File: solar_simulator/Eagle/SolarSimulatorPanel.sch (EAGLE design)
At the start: 82 parts, among them U1 Blue Driver, U2 Red Driver, U3 Green Driver, X1 MKDSN1,5/2-5,08

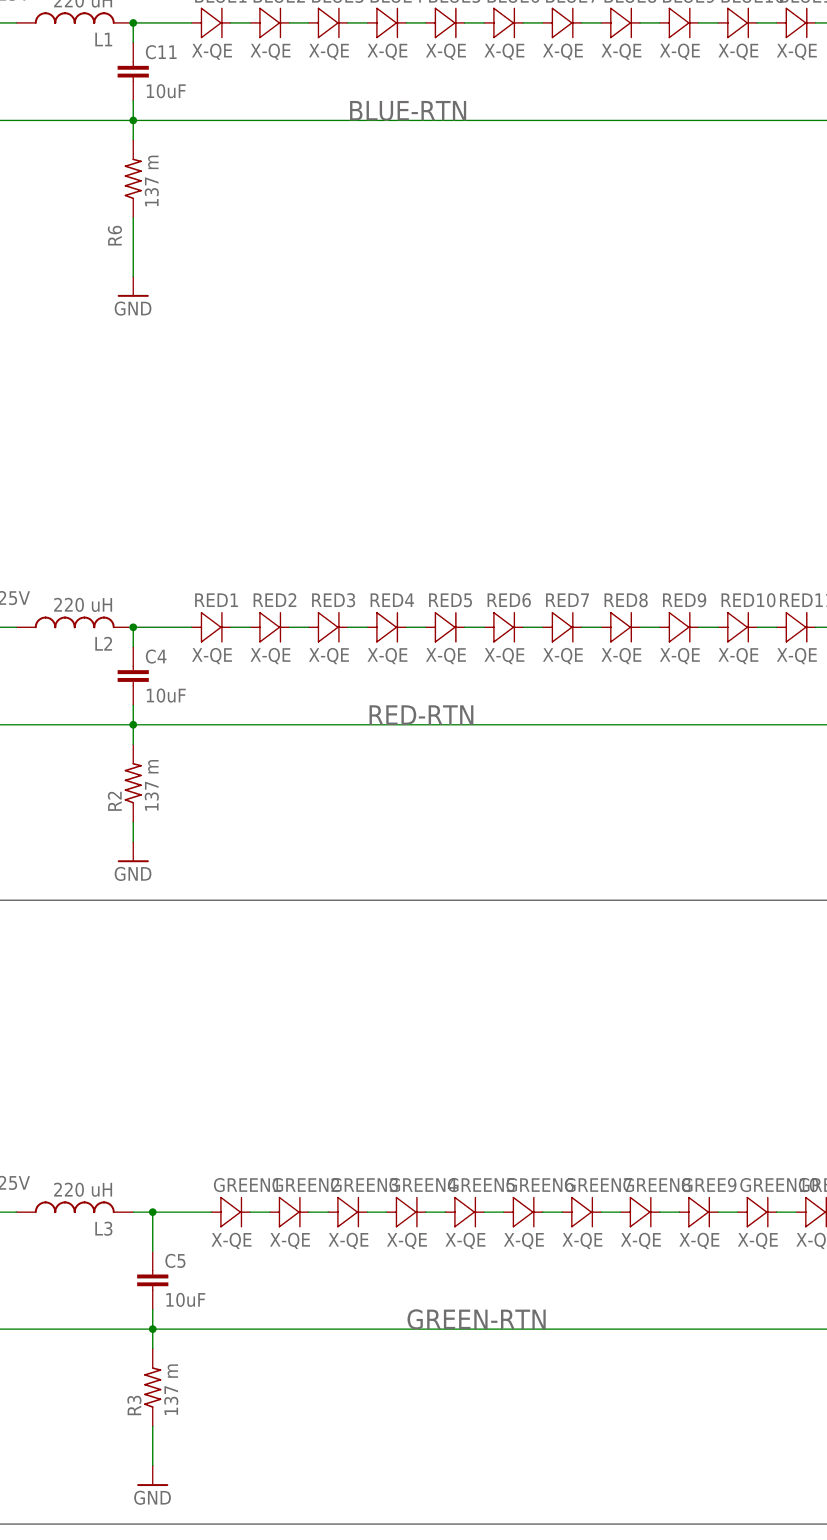
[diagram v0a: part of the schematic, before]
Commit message: added manufacturer informaton for temp sensors on solar sim, tweaks to 1u_panel, added very in progress driver for solar simulator.  Documentation inboud
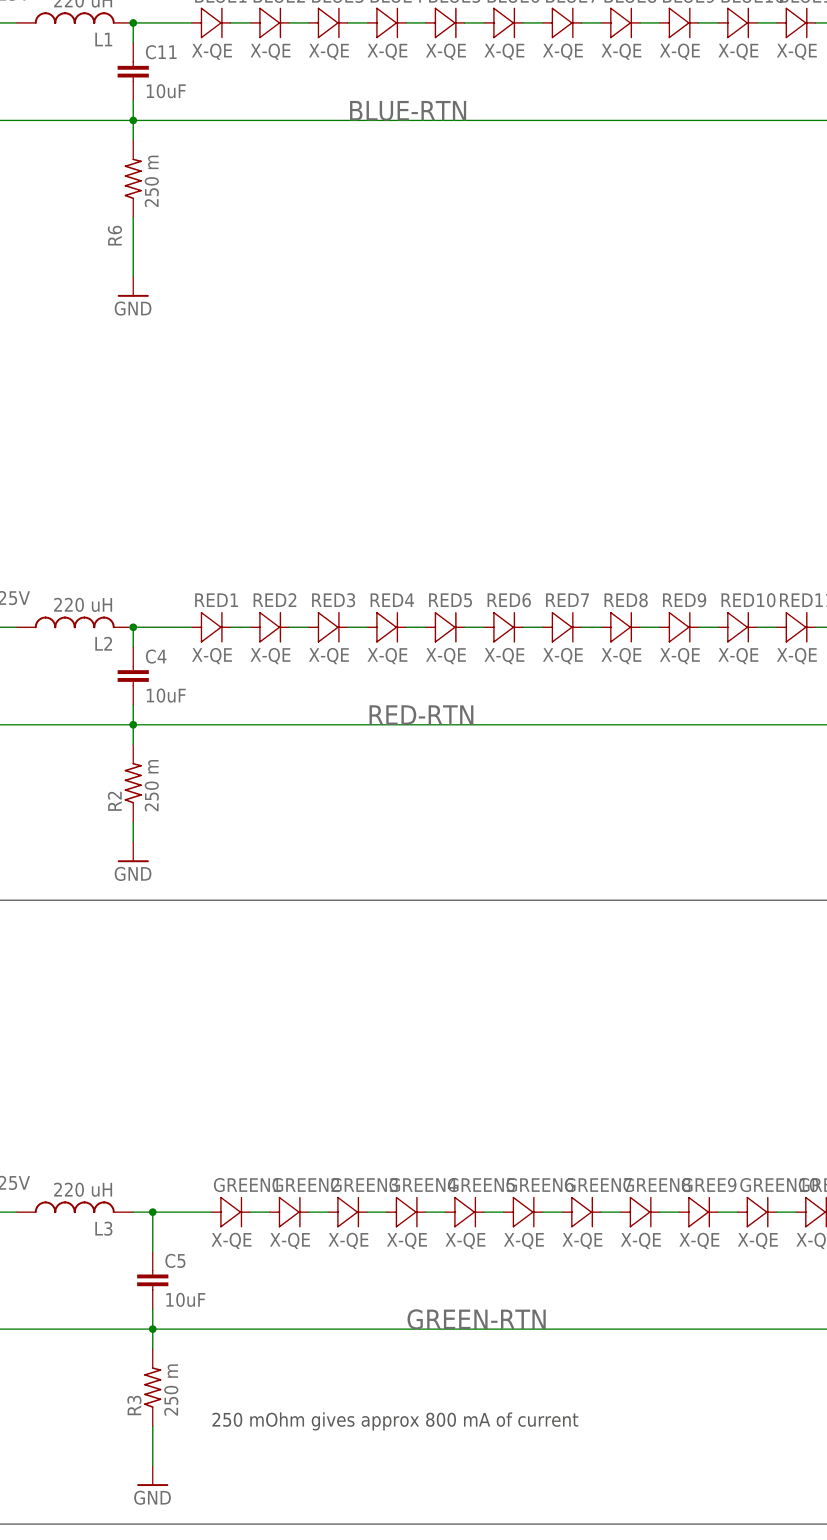
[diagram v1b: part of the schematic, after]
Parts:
- R2, R3, R6: value 137 m -> 250 m
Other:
- note added: "250 mOhm gives approx 800 mA of current"
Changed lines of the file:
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@@
 <?xml version="1.0" encoding="utf-8"?>
 <!DOCTYPE eagle SYSTEM "eagle.dtd">
-<eagle version="9.3.0">
+<eagle version="9.4.0">
 <drawing>
 <settings>
@@
 <part name="C1" library="rcl" library_urn="urn:adsk.eagle:library:334" deviceset="C-EU" device="C2220K" package3d_urn="urn:adsk.eagle:package:23687/2" value="1 uF 120V"/>
 <part name="C6" library="rcl" library_urn="urn:adsk.eagle:library:334" deviceset="C-EU" device="C2220K" package3d_urn="urn:adsk.eagle:package:23687/2" value="1 uF 120V"/>
-<part name="R6" library="rcl" library_urn="urn:adsk.eagle:library:334" deviceset="R-US_" device="R2010" package3d_urn="urn:adsk.eagle:package:23551/2" value="137 m"/>
-<part name="R2" library="rcl" library_urn="urn:adsk.eagle:library:334" deviceset="R-US_" device="R2010" package3d_urn="urn:adsk.eagle:package:23551/2" value="137 m"/>
-<part name="R3" library="rcl" library_urn="urn:adsk.eagle:library:334" deviceset="R-US_" device="R2010" package3d_urn="urn:adsk.eagle:package:23551/2" value="137 m"/>
+<part name="R6" library="rcl" library_urn="urn:adsk.eagle:library:334" deviceset="R-US_" device="R2010" package3d_urn="urn:adsk.eagle:package:23551/2" value="250 m"/>
+<part name="R2" library="rcl" library_urn="urn:adsk.eagle:library:334" deviceset="R-US_" device="R2010" package3d_urn="urn:adsk.eagle:package:23551/2" value="250 m"/>
+<part name="R3" library="rcl" library_urn="urn:adsk.eagle:library:334" deviceset="R-US_" device="R2010" package3d_urn="urn:adsk.eagle:package:23551/2" value="250 m"/>
 <part name="C3" library="oresat-rcl" deviceset="C-EU" device="0603-B-NOSILK" value="10nF 25V"/>
 <part name="C10" library="oresat-rcl" deviceset="C-EU" device="0603-B-NOSILK" value="10nF 25V"/>
@@
 <wire x1="142.24" y1="86.36" x2="93.98" y2="86.36" width="0.1524" layer="97"/>
 <wire x1="93.98" y1="86.36" x2="93.98" y2="38.1" width="0.1524" layer="97"/>
+<text x="274.32" y="50.8" size="1.778" layer="97">250 mOhm gives approx 800 mA of current</text>
 </plain>
 <instances>

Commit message: solar simulator documentation updates, preparing for R 2.0
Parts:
- RT1, RT3: DISTRIBUTOR (none) -> Digi-Key; DPN (none) -> 445-2550-1-ND; MPN (none) -> NTCG103JF103FT1
- RT2: DISTRIBUTOR (none) -> Digi-key; DPN (none) -> 445-2550-1-ND; MPN (none) -> NTCG103JF103FT1
- RT4: DISTRIBUTOR (none) -> digikey; DPN (none) -> 445-2550-1-ND; MPN (none) -> NTCG103JF103FT1
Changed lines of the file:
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@@
 <part name="GND17" library="supply1" library_urn="urn:adsk.eagle:library:371" deviceset="GND" device=""/>
 <part name="C11" library="oresat-rcl" deviceset="C-EU" device="1206-B" value="10uF"/>
-<part name="RT4" library="solarsim" deviceset="NTCTHERMISTER" device="" value="10K"/>
-<part name="RT3" library="solarsim" deviceset="NTCTHERMISTER" device="" value="10K"/>
-<part name="RT2" library="solarsim" deviceset="NTCTHERMISTER" device="" value="10K"/>
-<part name="RT1" library="solarsim" deviceset="NTCTHERMISTER" device="" value="10K"/>
+<part name="RT4" library="solarsim" deviceset="NTCTHERMISTER" device="" value="10K">
+<attribute name="DISTRIBUTOR" value="digikey"/>
+<attribute name="DPN" value="445-2550-1-ND"/>
+<attribute name="MPN" value="NTCG103JF103FT1"/>
+</part>
+<part name="RT3" library="solarsim" deviceset="NTCTHERMISTER" device="" value="10K">
+<attribute name="DISTRIBUTOR" value="Digi-Key"/>
+<attribute name="DPN" value="445-2550-1-ND"/>
+<attribute name="MPN" value="NTCG103JF103FT1"/>
+</part>
+<part name="RT2" library="solarsim" deviceset="NTCTHERMISTER" device="" value="10K">
+<attribute name="DISTRIBUTOR" value="Digi-key"/>
+<attribute name="DPN" value="445-2550-1-ND"/>
+<attribute name="MPN" value="NTCG103JF103FT1"/>
+</part>
+<part name="RT1" library="solarsim" deviceset="NTCTHERMISTER" device="" value="10K">
+<attribute name="DISTRIBUTOR" value="Digi-Key"/>
+<attribute name="DPN" value="445-2550-1-ND"/>
+<attribute name="MPN" value="NTCG103JF103FT1"/>
+</part>
 <part name="R11" library="oresat-rcl" deviceset="R-US_" device="0603-B-NOSILK" value="10k"/>
 <part name="C8" library="rcl" library_urn="urn:adsk.eagle:library:334" deviceset="C-EU" device="C2220K" package3d_urn="urn:adsk.eagle:package:23687/2" value="1 uF 120V"/>
@@
 <attribute name="NAME" x="122.809" y="201.93" size="1.778" layer="95" rot="R270"/>
 <attribute name="VALUE" x="120.65" y="201.93" size="1.778" layer="96" rot="R270"/>
+<attribute name="DISTRIBUTOR" x="116.84" y="198.12" size="1.778" layer="96" rot="R180" display="off"/>
+<attribute name="DPN" x="116.84" y="198.12" size="1.778" layer="96" rot="R180" display="off"/>
+<attribute name="MPN" x="116.84" y="198.12" size="1.778" layer="96" rot="R180" display="off"/>
 </instance>
 <instance part="RT3" gate="G$1" x="101.6" y="198.12" smashed="yes" rot="R180">
 <attribute name="NAME" x="107.569" y="201.93" size="1.778" layer="95" rot="R270"/>
 <attribute name="VALUE" x="105.41" y="201.93" size="1.778" layer="96" rot="R270"/>
+<attribute name="DISTRIBUTOR" x="101.6" y="198.12" size="1.778" layer="96" rot="R180" display="off"/>
+<attribute name="DPN" x="101.6" y="198.12" size="1.778" layer="96" rot="R180" display="off"/>
+<attribute name="MPN" x="101.6" y="198.12" size="1.778" layer="96" rot="R180" display="off"/>
 </instance>
 <instance part="RT2" gate="G$1" x="86.36" y="198.12" smashed="yes" rot="R180">
 <attribute name="NAME" x="92.329" y="201.93" size="1.778" layer="95" rot="R270"/>
 <attribute name="VALUE" x="90.17" y="201.93" size="1.778" layer="96" rot="R270"/>
+<attribute name="DISTRIBUTOR" x="86.36" y="198.12" size="1.778" layer="96" rot="R180" display="off"/>
+<attribute name="DPN" x="86.36" y="198.12" size="1.778" layer="96" rot="R180" display="off"/>
+<attribute name="MPN" x="86.36" y="198.12" size="1.778" layer="96" rot="R180" display="off"/>
 </instance>
 <instance part="RT1" gate="G$1" x="68.58" y="198.12" smashed="yes" rot="R180">
 <attribute name="NAME" x="74.549" y="201.93" size="1.778" layer="95" rot="R270"/>
 <attribute name="VALUE" x="72.39" y="201.93" size="1.778" layer="96" rot="R270"/>
+<attribute name="DISTRIBUTOR" x="68.58" y="198.12" size="1.778" layer="96" rot="R180" display="off"/>
+<attribute name="DPN" x="68.58" y="198.12" size="1.778" layer="96" rot="R180" display="off"/>
+<attribute name="MPN" x="68.58" y="198.12" size="1.778" layer="96" rot="R180" display="off"/>
 </instance>
 <instance part="R11" gate="R" x="116.84" y="213.36" smashed="yes" rot="R270">

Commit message: schematic for solar sim 2.0
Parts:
- removed U1: Blue Driver, solarsim:LM3404HVMA
- removed U2: Red Driver, solarsim:LM3404HVMA
- removed U3: Green Driver, solarsim:LM3404HVMA
- removed X1: MKDSN1,5/2-5,08, con-phoenix-508:MKDSN1,5/2-5,08
- added J1, J2: DCJ0202, con-jack:DCJ0202
- added R10, R15, R16, R17, R18, R19, R20, R21, R22, R23, R7, R8, R9: TBD, oresat-rcl:R-US_0402-A-NOSILK
- added R24, R25, R26, R27: (no value), oresat-rcl:R-US_0204/7
- added R28: 220, oresat-rcl:R-US_0402-A-NOSILK
- added R29: 10k, oresat-rcl:R-US_0402-A-NOSILK
- added U$1, U$2, U$3: TPS92512, U-TI-TPS92512-buck:TPS92512
- added U$4: MCP4728, U-Microchip-MCP4728-QuadDAC:MCP4728
- added U$5: AP2127, U-Diodes-AP2127-LDO:AP2127
- added U$6: NCH-SOT223, Q-MOSFET-NCH-SOT223:NCH-SOT223
- C1: value 1 uF 120V -> .1 u; device rcl:C-EUC2220K -> oresat-rcl:C-EU0402-A-NOSILK
- C10, C7: value 10nF 25V -> TBD; device oresat-rcl:C-EU0603-B-NOSILK -> oresat-rcl:C-EU0402-A-NOSILK
- C11: value 10uF -> TBD; device oresat-rcl:C-EU1206-B -> oresat-rcl:C-EU0402-A-NOSILK
- C12, C9: value 100nF 25V -> TBD; device oresat-rcl:C-EU0603-B-NOSILK -> oresat-rcl:C-EU0402-A-NOSILK
- C2: value 100n 25V -> .1u; device oresat-rcl:C-EU0603-B-NOSILK -> oresat-rcl:C-EU0402-A-NOSILK
- C3: value 10nF 25V -> .1u; device oresat-rcl:C-EU0603-B-NOSILK -> oresat-rcl:C-EU0402-A-NOSILK
- C4, C5: value 10uF -> .1u; device oresat-rcl:C-EU1206-B -> oresat-rcl:C-EU0402-A-NOSILK
- C6: value 1 uF 120V -> .1u; device rcl:C-EUC2220K -> oresat-rcl:C-EU0402-A-NOSILK
- C8: value 1 uF 120V -> TBD; device rcl:C-EUC2220K -> oresat-rcl:C-EU0402-A-NOSILK
- D1, D2, D3: value GF1 -> TBD; device diode:GF1 -> diode:ZENER-DIODESMB
- L1, L2, L3: value 220 uH -> TBD; device solarsim:FILTERINDUCTOR -> oresat-rcl:L-US1206-C; MFR Bourns -> (none); MPN SRR1260-221K -> (none)
- R1: value 597k -> 10k; device oresat-rcl:R-US_0603-B-NOSILK -> oresat-rcl:R-US_0402-A-NOSILK
- R2, R3: value 250 m -> 10k; device rcl:R-US_R2010 -> oresat-rcl:R-US_0402-A-NOSILK
- R4: value 597k -> 100k; device oresat-rcl:R-US_0603-B-NOSILK -> oresat-rcl:R-US_0402-A-NOSILK
- R5: value 597k -> TBD; device oresat-rcl:R-US_0603-B-NOSILK -> oresat-rcl:R-US_0402-A-NOSILK
- R6: value 250 m -> TBD; device rcl:R-US_R2010 -> oresat-rcl:R-US_0402-A-NOSILK
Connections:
- removed net BLUE-OUT: BLUE1.A, C11.1, L1.2
- removed net BLUE-RTN: BLUE15.C, C11.2, R6.2, U1.CS
- removed net D10/PWM_R: PCB1.D10, U2.DIM
- removed net D11/PWM_G: PCB1.D11/MOSI, U3.DIM
- removed net D9/PWM_B: PCB1.D9, U1.DIM
- removed net GREEN-RTN: C5.2, GREEN15.C, R3.2, U3.CS
- removed net GRN-OUT: C5.1, GREEN1.A, L3.2
- removed net RED-OUT: C4.1, L2.2, RED1.A
- removed net RED-RTN: C4.2, R2.2, RED15.C, U2.CS
- removed net VPP: C1.1, C6.1, C8.1, R1.2, R4.2, R5.2, U1.VIN, U2.VIN, U3.VIN, X1-1.KL
- new net +12: J1.3
- new net +3V3: PCB1.3V3, U$5.VIN
- new net +56V: J2.3
- new net N$24: C2.2, D2.C, L2.1, U$2.PH
- new net N$28: PCB1.D11/MOSI, R4.1, U$4.RDY/!BSY
- new net N$3: PCB1.A5, R1.1, U$4.SCL
- new net N$47: C1.1, U$3.BOOT
- new net N$51: C2.1, U$2.BOOT
- new net N$54: R16.2, U$2.ISENSE
- new net N$55: R17.2, U$3.ISENSE
- new net N$58: R15.2, U$1.ISENSE
- new net N$59: C8.2, R16.1, R19.2, RED15.C
- new net N$60: C8.1
- new net N$61: C9.2, GREEN15.C, R17.1, R20.2
- new net N$62: C9.1
- new net N$63: R21.2, U$2.RT/CLK
- new net N$64: U$1.IADJ, U$4.VOUTC
- new net N$65: R22.2, U$1.RT/CLK
- new net N$66: C10.1, U$2.COMP
- new net N$67: C11.1, U$1.COMP
- new net N$68: U$3.IADJ, U$4.VOUTA
- new net N$69: GREEN1.A, L1.2
- new net N$70: L2.2, RED1.A
- new net N$71: BLUE15.C, C7.2, R15.1, R18.2
- new net N$72: BLUE1.A, L3.2
- new net N$73: R24.1, U$6.S
- new net N$74: R24.2, R25.1
- new net N$75: R25.2, R26.1
- new net N$76: R26.2, R27.1
- new net N$78: R28.1, R29.2, U$6.G
- new net N$79: PCB1.D13/SCK, R28.2
- new net VCC: U$6.D
- new net VCC/2: C4.1, C5.1, R6.2, R8.2, U$2.VIN, U$3.VIN
- new net VCC/3: C6.1, R10.2, U$1.VIN
- net +5V: now also R1.2, R2.2, R3.2
- net GND: now also C10.2, C11.2, C4.2, C5.2, J1.1, J2.1, R18.1, R19.1, R20.1, R21.1, R22.1, R23.1, R27.2, R29.1, R5.1, R7.1, R9.1, U$1.GND, U$2.GND, U$3.GND, U$4.GND, U$5.GND; no longer C1.2, C2.2, C8.2, C9.2, R2.1, R3.1, R6.1, U1.GND, U2.GND, U3.GND, X1-2.KL
- net N$1: now also PCB1.A4, R2.1, U$4.SDA; no longer C7.2, D3.C, L3.1, U3.SW
- net N$18: now also U$2.IADJ, U$4.VOUTB; no longer R5.1, U1.RON
- net N$19: now also R23.2, U$3.RT/CLK; no longer R4.1, U3.RON
- net N$22: now also C3.2, C7.1, D3.C, L3.1, U$1.PH; no longer C3.1, U2.BOOT
- net N$25: now also C1.2, D1.C, L1.1, U$3.PH; no longer C3.2, D2.C, L2.1, U2.SW
- net N$32: now also PCB1.D12/MISO, R3.1, U$4.!LDAC; no longer C7.1, U3.BOOT
- net N$33: now also U$3.COMP; no longer U3.VCC
- net N$34: now also C3.1, U$1.BOOT; no longer C10.2, D1.C, L1.1, U1.SW
- net N$4: now also R4.2, U$4.VDD, U$5.VOUT; no longer C2.1, U2.VCC
- net N$52: now also R7.2, R8.1, U$2.UVLO; no longer C10.1, U1.BOOT
- net N$53: now also R10.1, R9.2, U$1.UVLO; no longer C9.1, U1.VCC
- net N$6: now also R5.2, R6.1, U$3.UVLO; no longer R1.1, U2.RON
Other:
- note added: "Blue"
- note added: "Green"
- note added: "Incandescent"
- note added: "Power In (56V and 12V)"
- note added: "Red"
- note added: "TH Resistors are place holder for Halogen bulbs"
- note removed: "250 mOhm gives approx 800 mA of current"
- note removed: "BLUE"
- note removed: "GREEN"
- note removed: "POWER IN (60V 3A)"
- note removed: "RED"
- moved on the sheet: BLUE1, BLUE10, BLUE11, BLUE12, BLUE13, BLUE14, BLUE15, BLUE2, BLUE3, BLUE4, BLUE5, BLUE6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

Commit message: forgot a pullup
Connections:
- new net N$80: U$5.!SHDN, U$5.VIN
- net +3V3: no longer U$5.VIN
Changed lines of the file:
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@@
 <pinref part="+3V1" gate="G$1" pin="+3V3"/>
-</segment>
-<segment>
-<pinref part="U$5" gate="G$1" pin="VIN"/>
-<pinref part="+3V2" gate="G$1" pin="+3V3"/>
-<wire x1="129.286" y1="169.926" x2="129.286" y2="172.72" width="0.1524" layer="91"/>
 </segment>
 </net>
@@
 </segment>
 </net>
+<net name="N$80" class="0">
+<segment>
+<pinref part="U$5" gate="G$1" pin="VIN"/>
+<pinref part="+3V2" gate="G$1" pin="+3V3"/>
+<wire x1="129.286" y1="169.926" x2="129.286" y2="172.72" width="0.1524" layer="91"/>
+<pinref part="U$5" gate="G$1" pin="!SHDN"/>
+<wire x1="116.332" y1="154.686" x2="111.76" y2="154.686" width="0.1524" layer="91"/>
+<wire x1="129.286" y1="169.926" x2="111.76" y2="169.926" width="0.1524" layer="91"/>
+<wire x1="111.76" y1="169.926" x2="111.76" y2="154.686" width="0.1524" layer="91"/>
+<junction x="129.286" y="169.926"/>
+</segment>
+</net>

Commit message: added solar simulator rev 2.0, moved eagle files to oresat eagle repo
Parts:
- removed R24, R25, R26, R27: (no value), oresat-rcl:R-US_0204/7
- added TP1, TP10, TP11, TP12, TP13, TP14, TP15, TP16, TP17, TP18, TP19, TP2, TP20, TP21, TP22, TP23, TP24, TP25, TP26, TP3, TP4, TP5, TP6, TP7, TP8, TP9: TEST-POINT, Tova:TEST-POINT
- added U$10, U$7, U$8, U$9: HL_G4BULB, HL_HalogenBulb_G4Base:HL_G4BULB
- BLUE1, BLUE10, BLUE11, BLUE12, BLUE13, BLUE14, BLUE15, BLUE2, BLUE3, BLUE4, BLUE5, BLUE6, BLUE7, BLUE8, BLUE9, GREE9, GREEN1, GREEN10, GREEN11, GREEN12, GREEN13, GREEN14, GREEN15, GREEN2, GREEN3, GREEN4, GREEN5, GREEN6, GREEN7, GREEN8, RED1, RED10, RED11, RED12, RED13, RED14, RED15, RED2, RED3, RED4, RED5, RED6, RED7, RED8, RED9: device solarsim:X-QE -> D-Cree-XQE-LED:X-QE
- C10, C11, C12: value TBD -> .1u
- C7, C8, C9: value TBD -> .15u
- D1, D2, D3: value TBD -> (none)
- L1, L2, L3: value TBD -> 170u; device oresat-rcl:L-US1206-C -> L_Wurst_7447709681:7447709681
- R21, R22, R23: value TBD -> 11k
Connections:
- removed net +12: J1.3
- removed net +56V: J2.3
- removed net N$60: C8.1
- removed net N$62: C9.1
- net +3V3: now also TP17.1
- net +5V: now also TP18.1
- net A0: now also TP1.1
- net A1: now also TP2.1
- net A2: now also TP3.1
- net A3: now also TP4.1
- net GND: now also U$10.P$2; no longer R27.2
- net N$1: now also TP20.1
- net N$18: now also TP7.1
- net N$22: now also TP26.1
- net N$24: now also C8.1, TP25.1
- net N$25: now also C9.1, TP24.1
- net N$28: now also TP14.1
- net N$3: now also TP19.1
- net N$32: now also TP5.1
- net N$4: now also TP16.1
- net N$52: now also TP10.1
- net N$53: now also TP11.1
- net N$59: now also TP21.1
- net N$6: now also TP9.1
- net N$61: now also TP23.1
- net N$64: now also TP8.1
- net N$68: now also TP6.1
- net N$71: now also TP22.1
- net N$73: now also U$7.P$1; no longer R24.1
- net N$74: now also U$7.P$2, U$8.P$1; no longer R24.2, R25.1
- net N$75: now also U$8.P$2, U$9.P$1; no longer R25.2, R26.1
- net N$76: now also U$10.P$1, U$9.P$2; no longer R26.2, R27.1
- net N$78: now also TP15.1
- net VCC: now also J1.3, TP13.1
- net VCC/2: now also J2.3, TP12.1
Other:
- note removed: "TH Resistors are place holder for Halogen bulbs"
- moved on the sheet: C7, C9
